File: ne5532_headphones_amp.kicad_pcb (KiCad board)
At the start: 2 copper layers, 84.8 x 53.6 mm, 35 parts, among them J1 JACK_TRS_3PINS, J2 JACK_TRS_3PINS, J3 Conn_01x03_Male, Q1 BD140, Q2 BD139, Q3 BD139, Q4 BD140, U1 NE5532

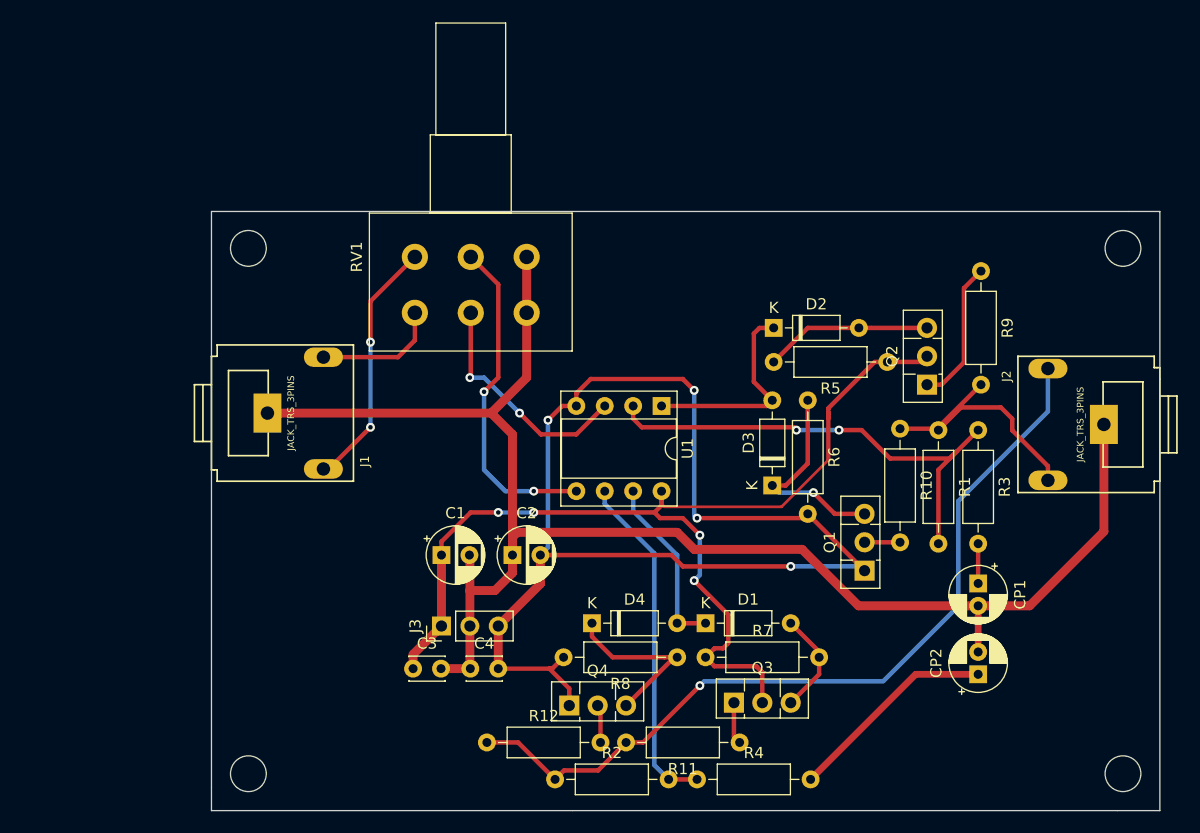
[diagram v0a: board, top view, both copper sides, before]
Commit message: more compact layout
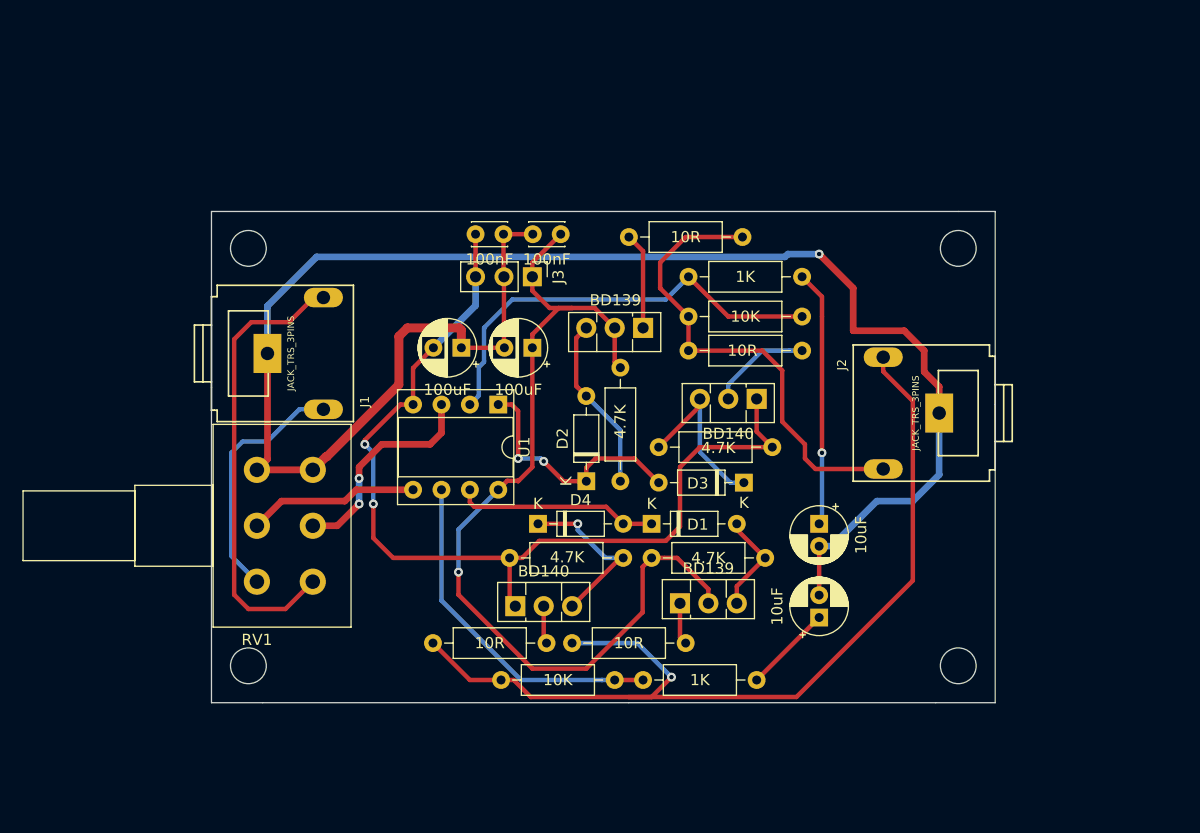
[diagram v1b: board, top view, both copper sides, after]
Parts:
- removed the   at (60.2, 116.1)
- removed the   at (138.4, 116.1)
- removed the   at (138.4, 69.1)
- removed Q2: BD139, Package_TO_SOT_THT:TO-126-3_Vertical
- removed R1: 10K, Resistor_THT:R_Axial_DIN0207_L6.3mm_D2.5mm_P10.16mm_Horizontal
- removed R10, R11, R9: 10R, Resistor_THT:R_Axial_DIN0207_L6.3mm_D2.5mm_P10.16mm_Horizontal
- removed R3: 1K, Resistor_THT:R_Axial_DIN0207_L6.3mm_D2.5mm_P10.16mm_Horizontal
- removed R5, R7: 4.7K, Resistor_THT:R_Axial_DIN0207_L6.3mm_D2.5mm_P10.16mm_Horizontal
- added  : MountingHole_3.2mm_M3_DIN965, MountingHole:MountingHole_3.2mm_M3_DIN965, F.Cu at (60.2, 106.4)
- added  : MountingHole_3.2mm_M3_DIN965, MountingHole:MountingHole_3.2mm_M3_DIN965, F.Cu at (123.7, 106.4)
- added  : MountingHole_3.2mm_M3_DIN965, MountingHole:MountingHole_3.2mm_M3_DIN965, F.Cu at (123.7, 69.1)
- added 10K: 10K, Resistor_THT:R_Axial_DIN0207_L6.3mm_D2.5mm_P10.16mm_Horizontal, F.Cu at (99.6, 75.2)
- added 10R: 10R, Resistor_THT:R_Axial_DIN0207_L6.3mm_D2.5mm_P10.16mm_Horizontal, F.Cu at (94.2, 68.1)
- added 10R: 10R, Resistor_THT:R_Axial_DIN0207_L6.3mm_D2.5mm_P10.16mm_Horizontal, F.Cu at (99.6, 78.2)
- added 10R: 10R, Resistor_THT:R_Axial_DIN0207_L6.3mm_D2.5mm_P10.16mm_Horizontal, F.Cu at (99.3, 104.4)
- added 1K: 1K, Resistor_THT:R_Axial_DIN0207_L6.3mm_D2.5mm_P10.16mm_Horizontal, F.Cu at (99.6, 71.6)
- added 4.7K: 4.7K, Resistor_THT:R_Axial_DIN0207_L6.3mm_D2.5mm_P10.16mm_Horizontal, F.Cu at (93.5, 79.8)
- added 4.7K: 4.7K, Resistor_THT:R_Axial_DIN0207_L6.3mm_D2.5mm_P10.16mm_Horizontal, F.Cu at (96.3, 96.8)
- added BD139: BD139, Package_TO_SOT_THT:TO-126-3_Vertical, F.Cu at (95.5, 76.2)
- moved 100nF 41.0 mm to (88.1, 67.8), turned to 180 degrees
- moved 100nF 39.0 mm to (83.0, 67.8), turned to 180 degrees
- moved J3 32.3 mm to (85.6, 71.6), turned to 270 degrees
- moved RV1 30.7 mm to (61.0, 88.9), turned to 180 degrees
- moved D2 21.7 mm to (90.4, 89.9), turned to 90 degrees
- moved 100uF 20.2 mm to (85.6, 78.0), turned to 180 degrees
- moved 100uF 19.1 mm to (79.2, 78.0), turned to 180 degrees
- moved BD140 18.1 mm to (105.7, 82.5), turned to 180 degrees
- moved 10uF 15.2 mm to (111.3, 93.7)
- moved 10uF 15.1 mm to (111.3, 102.1)
- moved J2 14.8 mm to (120.4, 83.8)
- moved U1 14.6 mm to (82.5, 83.1)
- moved 4.7K 14.0 mm to (96.9, 86.9), turned to 0 degrees
- moved 10R 10.1 mm to (76.7, 104.4)
- moved 4.7K 10.1 mm to (93.7, 96.8)
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- renumbered C3 to 100nF, C4 to 100nF, C1 to 100uF, C2 to 100uF, R2 to 10K, R12 to 10R, CP1 to 10uF, CP2 to 10uF, R4 to 1K, R6 to 4.7K, R8 to 4.7K, Q3 to BD139, Q1 to BD140, Q4 to BD140
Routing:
- net JACK_R: track 11.3 -> 41.0 mm
- net -9V: track 108.4 -> 85.3 mm, vias 4 -> 2
- net Net-(CP1-Pad1): track 3.56 -> 22.9 mm, vias 0 -> 1
- net JACK_OUT_R: track 24.0 -> 42.5 mm
- net Net-(RV1-Pad2): track 29.6 -> 15.3 mm, vias 2 -> 0
- net GND: track 141.5 -> 155.4 mm, vias 0 -> 1
- net Net-(CP2-Pad1): track 18.9 -> 7.90 mm
- net +9V: track 94.5 -> 83.8 mm, vias 4 -> 1
- net JACK_OUT_T: track 74.5 -> 85.0 mm
- net Net-(R1-Pad2): track 48.5 -> 39.2 mm, vias 2 -> 0
- net Net-(Q1-Pad2): track 3.17 -> 9.14 mm
- net Net-(Q2-Pad1): track 12.9 -> 8.65 mm
- net Net-(D2-Pad1): track 18.8 -> 22.1 mm, vias 0 -> 2
- net Net-(D3-Pad1): track 18.9 -> 15.7 mm, vias 1 -> 0
- net Net-(D1-Pad1): track 16.0 -> 18.2 mm
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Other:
- board size 84.8 x 53.6 mm -> 70.1 x 43.9 mm

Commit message: add logo
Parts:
- added REF**: OSHW-Logo2_7.3x6mm_SilkScreen, Symbol:OSHW-Logo2_7.3x6mm_SilkScreen, F.Cu at (116.5, 97.9)
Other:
- board text added: "https://github.com/jovan3/ne5532_headphones_amp"

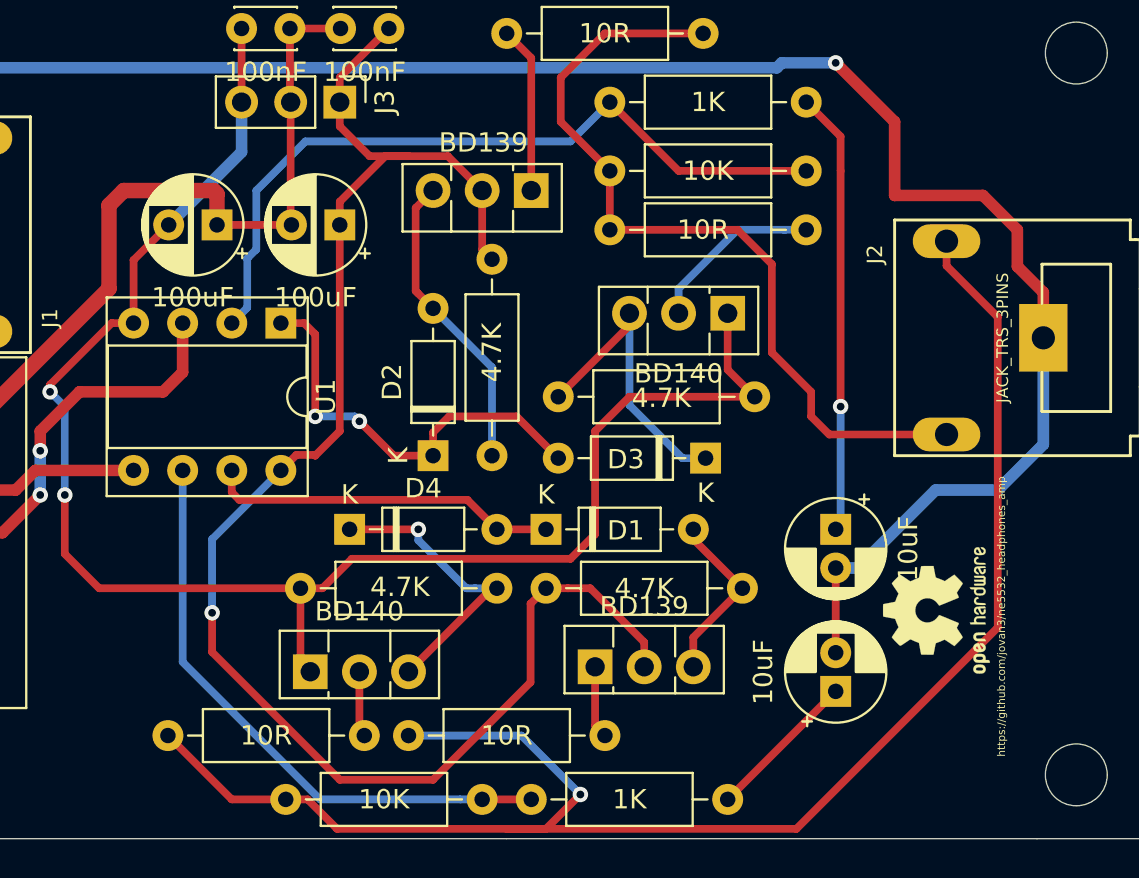
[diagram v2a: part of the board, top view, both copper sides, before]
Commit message: fix some square edged tracks, cleanup
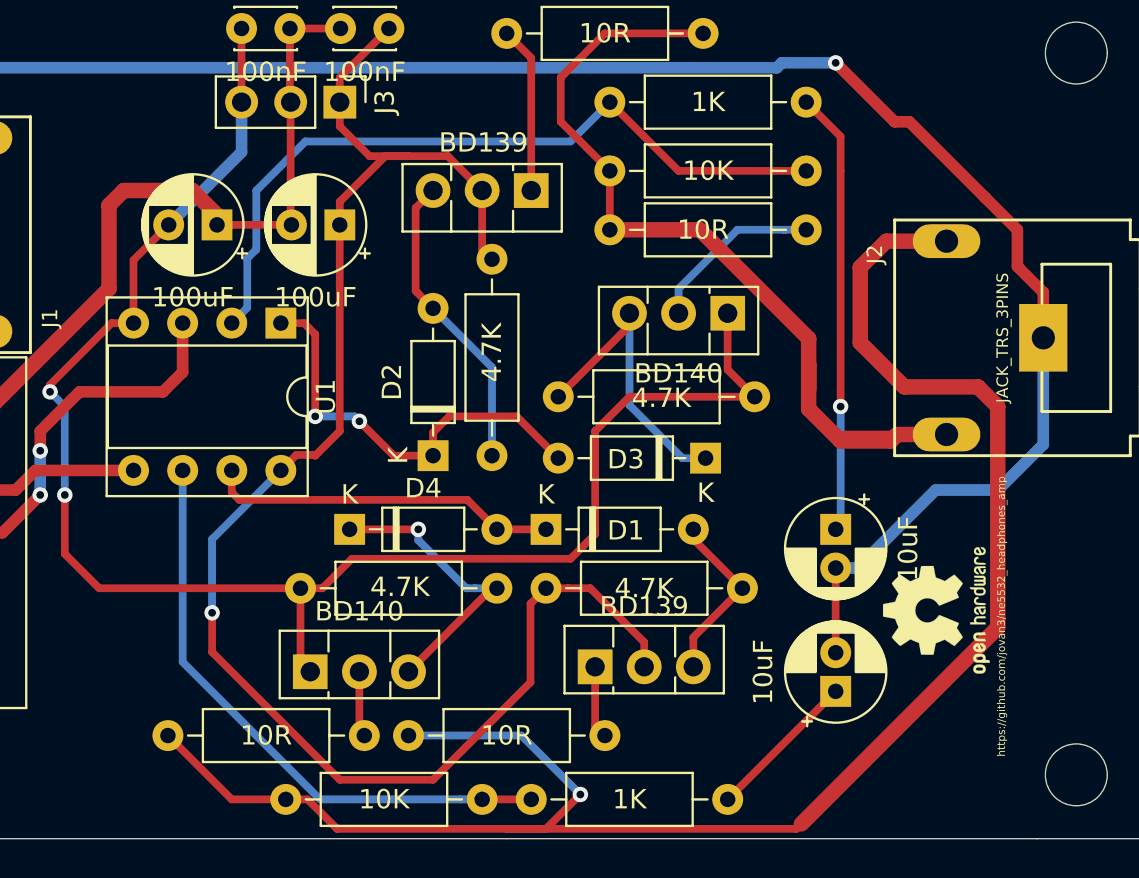
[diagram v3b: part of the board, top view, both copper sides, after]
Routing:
- net JACK_OUT_R: track 42.5 -> 51.6 mm
- net JACK_OUT_T: track 85.0 -> 92.8 mm
- net GND: track 155.4 -> 152.7 mm
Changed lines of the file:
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@@
     (thickness 1.6)
     (drawings 11)
-    (tracks 219)
+    (tracks 231)
     (zones 0)
     (modules 36)
@@
   )
   (setup
-    (last_trace_width 0.6)
+    (last_trace_width 0.8)
     (user_trace_width 0.4)
     (user_trace_width 0.6)
@@
   (segment (start 73.66 81.28) (end 73.66 76.962) (width 0.8) (layer F.Cu) (net 1))
   (segment (start 73.66 76.962) (end 74.422 76.2) (width 0.8) (layer F.Cu) (net 1))
-  (segment (start 79.07 76.2) (end 79.248 76.378) (width 0.8) (layer F.Cu) (net 1))
-  (segment (start 79.248 76.378) (end 79.248 77.978) (width 0.8) (layer F.Cu) (net 1))
-  (segment (start 74.422 76.2) (end 79.07 76.2) (width 0.8) (layer F.Cu) (net 1))
   (segment (start 121.992 81.47) (end 120.65 80.128) (width 0.6) (layer F.Cu) (net 1))
   (segment (start 121.992 83.82) (end 121.992 81.47) (width 0.6) (layer F.Cu) (net 1))
   (segment (start 120.65 80.128) (end 120.65 78.232) (width 0.6) (layer F.Cu) (net 1))
-  (segment (start 120.65 78.232) (end 118.872 76.454) (width 0.6) (layer F.Cu) (net 1))
-  (segment (start 118.872 76.454) (end 114.3 76.454) (width 0.6) (layer F.Cu) (net 1))
-  (segment (start 114.3 76.454) (end 114.3 72.644) (width 0.6) (layer F.Cu) (net 1))
   (via (at 111.252 69.596) (size 0.8) (drill 0.4) (layers F.Cu B.Cu) (net 1))
   (segment (start 114.3 72.644) (end 111.252 69.596) (width 0.6) (layer F.Cu) (net 1))
@@
   (segment (start 121.992 89.336) (end 121.992 83.82) (width 0.6) (layer B.Cu) (net 1))
   (segment (start 119.634 91.694) (end 121.992 89.336) (width 0.6) (layer B.Cu) (net 1))
+  (segment (start 115.062 72.644) (end 118.999 76.581) (width 0.6) (layer F.Cu) (net 1))
+  (segment (start 114.3 72.644) (end 115.062 72.644) (width 0.6) (layer F.Cu) (net 1))
+  (segment (start 120.65 78.232) (end 118.999 76.581) (width 0.6) (layer F.Cu) (net 1))
+  (segment (start 118.999 76.581) (end 118.872 76.454) (width 0.6) (layer F.Cu) (net 1))
+  (segment (start 79.248 77.978) (end 79.248 77.47) (width 0.8) (layer F.Cu) (net 1))
+  (segment (start 77.978 76.2) (end 74.422 76.2) (width 0.8) (layer F.Cu) (net 1))
+  (segment (start 79.248 77.47) (end 77.978 76.2) (width 0.8) (layer F.Cu) (net 1))
   (segment (start 83.349999 89.878001) (end 82.55 90.678) (width 0.4) (layer F.Cu) (net 2))
   (segment (start 84.290001 89.878001) (end 83.349999 89.878001) (width 0.4) (layer F.Cu) (net 2))
@@
   (segment (start 97.028 70.358) (end 97.028 72.644) (width 0.4) (layer F.Cu) (net 14))
   (segment (start 99.568 75.184) (end 99.568 78.232) (width 0.4) (layer F.Cu) (net 14))
-  (segment (start 107.95 80.01) (end 107.95 84.582) (width 0.4) (layer F.Cu) (net 14))
   (segment (start 109.982 86.614) (end 109.982 87.884) (width 0.4) (layer F.Cu) (net 14))
   (segment (start 110.918 88.82) (end 116.986 88.82) (width 0.4) (layer F.Cu) (net 14))
-  (segment (start 99.568 78.232) (end 106.172 78.232) (width 0.4) (layer F.Cu) (net 14))
   (segment (start 109.982 87.884) (end 110.918 88.82) (width 0.4) (layer F.Cu) (net 14))
-  (segment (start 106.172 78.232) (end 107.95 80.01) (width 0.4) (layer F.Cu) (net 14))
-  (segment (start 107.95 84.582) (end 109.982 86.614) (width 0.4) (layer F.Cu) (net 14))
+  (segment (start 104.226002 78.232) (end 109.855 83.860998) (width 0.8) (layer F.Cu) (net 14))
+  (segment (start 99.568 78.232) (end 104.226002 78.232) (width 0.8) (layer F.Cu) (net 14))
+  (segment (start 109.855 86.487) (end 109.982 86.614) (width 0.4) (layer F.Cu) (net 14))
+  (segment (start 109.855 87.503) (end 109.855 85.217) (width 0.8) (layer F.Cu) (net 14))
+  (segment (start 109.855 85.217) (end 109.855 86.487) (width 0.8) (layer F.Cu) (net 14))
+  (segment (start 109.855 83.860998) (end 109.855 85.217) (width 0.8) (layer F.Cu) (net 14))
+  (segment (start 116.986 88.82) (end 114.436 88.82) (width 0.8) (layer F.Cu) (net 14))
+  (segment (start 114.102 89.154) (end 111.506 89.154) (width 0.8) (layer F.Cu) (net 14))
+  (segment (start 114.436 88.82) (end 114.102 89.154) (width 0.8) (layer F.Cu) (net 14))
+  (segment (start 111.506 89.154) (end 109.855 87.503) (width 0.8) (layer F.Cu) (net 14))
   (segment (start 80.01 107.696) (end 82.804 107.696) (width 0.4) (layer F.Cu) (net 15))
   (segment (start 76.708 104.394) (end 80.01 107.696) (width 0.4) (layer F.Cu) (net 15))
   (segment (start 83.93537 107.696) (end 85.45937 109.22) (width 0.4) (layer F.Cu) (net 15))
   (segment (start 82.804 107.696) (end 83.93537 107.696) (width 0.4) (layer F.Cu) (net 15))
-  (segment (start 109.22 109.22) (end 119.634 98.806) (width 0.4) (layer F.Cu) (net 15))
-  (segment (start 116.986 80.095) (end 116.986 78.82) (width 0.4) (layer F.Cu) (net 15))
-  (segment (start 119.634 82.743) (end 116.986 80.095) (width 0.4) (layer F.Cu) (net 15))
-  (segment (start 119.634 98.806) (end 119.634 82.743) (width 0.4) (layer F.Cu) (net 15))
   (segment (start 89.154 104.394) (end 94.996 104.394) (width 0.4) (layer B.Cu) (net 15))
   (via (at 98.044 107.442) (size 0.8) (drill 0.4) (layers F.Cu B.Cu) (net 15))
@@
   (segment (start 96.266 109.22) (end 94.234 109.22) (width 0.4) (layer F.Cu) (net 15))
   (segment (start 94.234 109.22) (end 109.22 109.22) (width 0.4) (layer F.Cu) (net 15))
+  (segment (start 119.634 87.376) (end 119.634 98.806) (width 0.8) (layer F.Cu) (net 15))
+  (segment (start 118.618 86.36) (end 119.634 87.376) (width 0.8) (layer F.Cu) (net 15))
+  (segment (start 116.986 78.82) (end 113.872 78.82) (width 0.8) (layer F.Cu) (net 15))
+  (segment (start 119.634 98.806) (end 109.474 108.966) (width 0.8) (layer F.Cu) (net 15))
+  (segment (start 113.872 78.82) (end 112.522 80.17) (width 0.8) (layer F.Cu) (net 15))
+  (segment (start 112.522 84.074) (end 114.808 86.36) (width 0.8) (layer F.Cu) (net 15))
+  (segment (start 109.22 109.22) (end 109.474 108.966) (width 0.4) (layer F.Cu) (net 15))
+  (segment (start 112.522 80.17) (end 112.522 84.074) (width 0.8) (layer F.Cu) (net 15))
+  (segment (start 114.808 86.36) (end 118.618 86.36) (width 0.8) (layer F.Cu) (net 15))
   (segment (start 108.59663 78.232) (end 109.728 78.232) (width 0.4) (layer B.Cu) (net 16))
   (segment (start 106.169208 78.232) (end 108.59663 78.232) (width 0.4) (layer B.Cu) (net 16))
